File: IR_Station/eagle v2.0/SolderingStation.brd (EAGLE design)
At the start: 160 x 100 mm, 104 parts, among them IC1 LM317, U1 MSP340G2443, U2 UPD166010, U3 MCP6V08, U4 UPD166010, U5 MCP6V08, U6 ADS1115IDGST

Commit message: Update linse from all pins! some features :)
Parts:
- added C15, C8: 1nF, adi_v1.2:0805
- added JP11: (no value), pinhead:1X02
- added JP15: (no value), pinhead:1X01
- added JP16: (no value), pinhead:1X05
- added R25: 87R, adi_v1.2:0805
- added R34: 0R, adi_v1.2:0805
- added U$12: (no value), Serghei IR station:UNDEF1
- JP1: device pinhead:1X04/90 -> pinhead:1X02
- JP6: device pinhead:1X06 -> pinhead:1X04
- moved JP1 16.3 mm to (75.2, 80.8), turned to 90 degrees
- moved LED1 3.90 mm to (77.0, 76.5), turned to 180 degrees
- moved R21 3.15 mm to (75.9, 85.3)
- moved JP6 2.51 mm to (57.0, 23.0)
- moved R19 2.31 mm to (78.8, 81.8), turned to 90 degrees
- moved R9 1.80 mm to (82.1, 81.8)
- moved JP7 0.71 mm to (54.4, 45.5)
- moved JP10 0.50 mm to (64.2, 45.5)
- moved JP9 0.50 mm to (83.0, 45.5)
- moved R18 0.50 mm to (64.0, 42.7)
- moved U1 0.50 mm to (67.3, 31.8)
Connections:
- new net N$2222: JP1.1, LED1.A
- new net N$37: C8.1, U$12.P$2, U1.6
- new net N$39: C15.1, U$12.P$1, U1.7
- new net N$45: JP15.1, R25.1
- new net N$46: CLH1.INPUT, R34.1
- net +3V3_220V: now also JP16.2; no longer JP1.1
- net 24V_CS_UC: now also JP6.4; no longer JP6.6
- net 24V_PWM: now also R25.2, R34.2; no longer CLH1.INPUT
- net DATA_DISPLAY: now also JP6.1; no longer JP6.3
- net GND_220V: now also JP16.5; no longer JP1.4
- net GND_UC: now also C15.2, C8.2
- net N$15: now also JP16.4; no longer JP1.3
- net N$17: now also JP1.2, JP16.1; no longer LED1.A
- net N$36: now also JP16.3; no longer JP1.2
- net RX: now also JP6.3; no longer JP6.5
- net TIP_TEMP1_UC: now also JP11.2, U$12.P$3; no longer JP6.2, U1.6
- net TIP_TEMP2_UC: now also JP11.1, U$12.P$4; no longer JP6.1, U1.7
- net TX: now also JP6.2; no longer JP6.4
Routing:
- net N$37: track 0.00 -> 17.7 mm
- net N$39: track 0.00 -> 15.3 mm
- net N$17: track 4.49 -> 17.8 mm
- net N$46: track 0.00 -> 10.6 mm
- net N$26: track 180.0 -> 170.0 mm
- net TIP_TEMP1_UC: track 7.35 -> 3.31 mm
- net N$17_UC: track 0.00 -> 3.25 mm, vias 0 -> 2
- net N$2222: track 0.00 -> 2.96 mm
- net N$45: track 0.00 -> 2.65 mm
- net TIP_TEMP2_UC: track 6.08 -> 4.03 mm
- net N$25: track 102.0 -> 103.8 mm
- net +3V3_UC: track 106.1 -> 107.7 mm
- net N$10: track 16.0 -> 14.5 mm
- net GND_ST_LIPIT: track 168.3 -> 169.8 mm
- net N$6: track 8.49 -> 7.21 mm
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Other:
- board text added: "FRONT"
- board text added: "LED"
- board text added: "PANEL"
- board text added: "PWM_220V_LED"

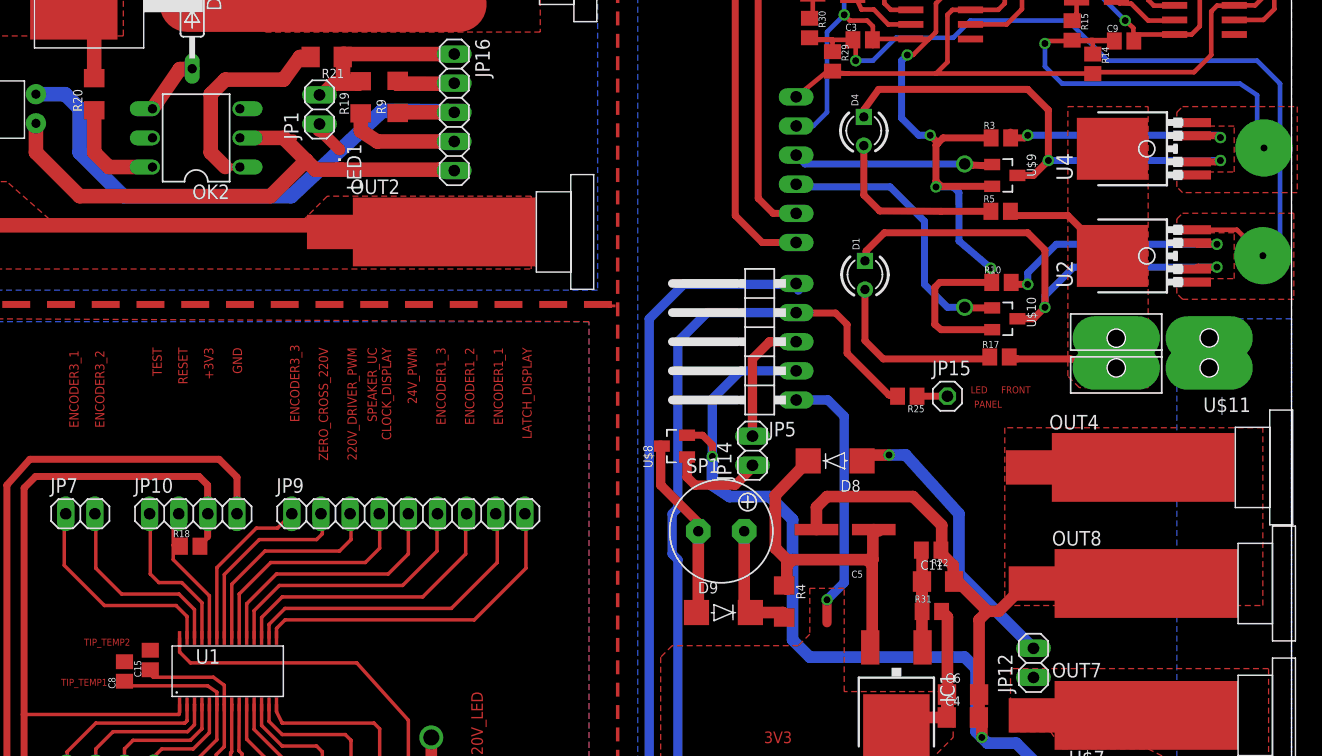
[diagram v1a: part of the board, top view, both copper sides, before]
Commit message: PDF, and correct few lines.
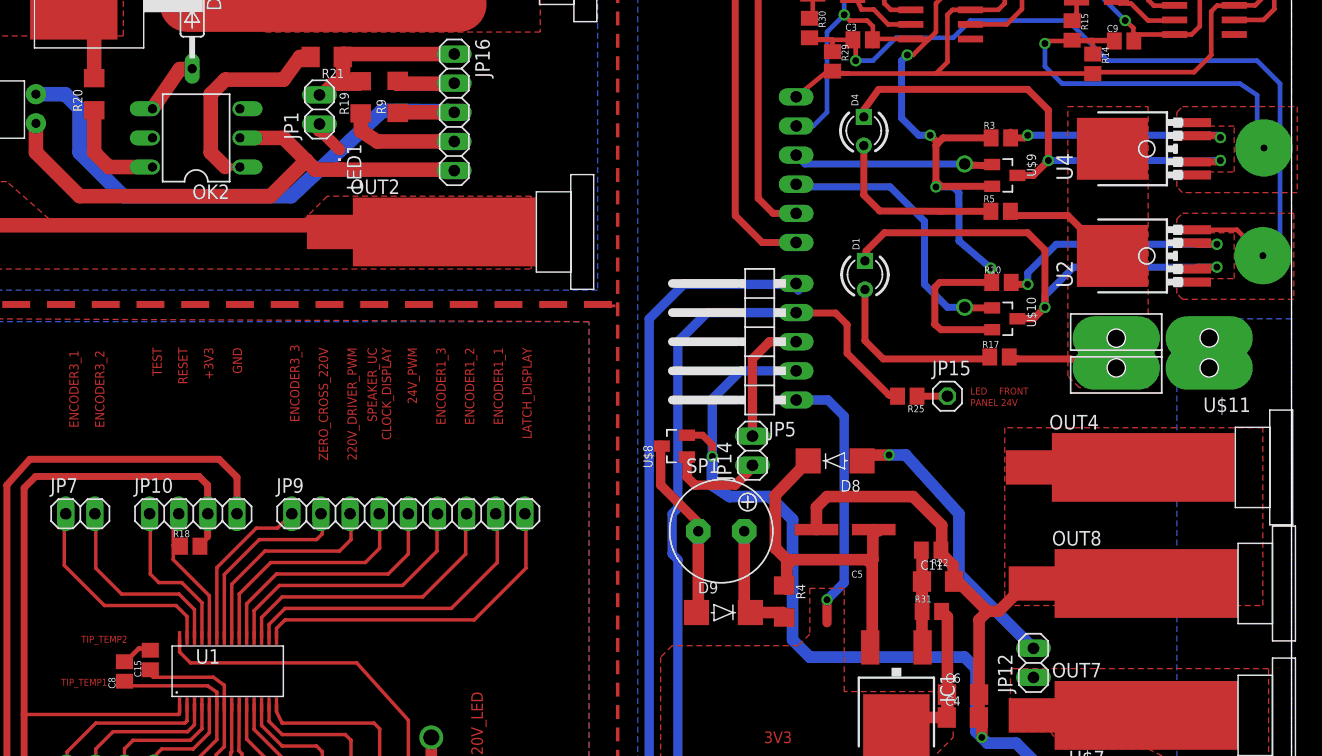
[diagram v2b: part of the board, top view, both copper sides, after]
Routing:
- net GND_UC: track 154.6 -> 157.5 mm
- net GND_220V: track 52.7 -> 52.0 mm
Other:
- board text added: "PANEL 24V"
- board text removed: "PANEL"
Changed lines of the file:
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@@
 <layer number="14" name="Route14" color="1" fill="6" visible="yes" active="yes"/>
 <layer number="15" name="Route15" color="4" fill="6" visible="yes" active="yes"/>
-<layer number="16" name="Bottom" color="1" fill="1" visible="yes" active="yes"/>
+<layer number="16" name="Bottom" color="1" fill="1" visible="no" active="yes"/>
 <layer number="17" name="Pads" color="2" fill="1" visible="yes" active="yes"/>
 <layer number="18" name="Vias" color="2" fill="1" visible="yes" active="yes"/>
@@
 <rectangle x1="0" y1="31" x2="44.25" y2="64" layer="16"/>
 <text x="56.75" y="30.5" size="0.6096" layer="1" font="vector" align="bottom-right">TIP_TEMP1</text>
-<text x="58.75" y="34" size="0.6096" layer="1" font="vector" align="bottom-right">TIP_TEMP2</text>
-<text x="133.5" y="56" size="0.6096" layer="1" font="vector" align="bottom-right">LED</text>
-<text x="137.25" y="56" size="0.6096" layer="1" font="vector" align="bottom-right">FRONT</text>
-<text x="134.75" y="54.75" size="0.6096" layer="1" font="vector" align="bottom-right">PANEL</text>
+<text x="58.5" y="34.25" size="0.6096" layer="1" font="vector" align="bottom-right">TIP_TEMP2</text>
+<text x="132" y="56.5" size="0.6096" layer="1" font="vector" rot="R180" align="bottom-right">LED</text>
+<text x="134.5" y="56.5" size="0.6096" layer="1" font="vector" rot="R180" align="bottom-right">FRONT</text>
+<text x="132" y="55.5" size="0.6096" layer="1" font="vector" rot="R180" align="bottom-right">PANEL 24V</text>
 <text x="89.5" y="30" size="1.016" layer="1" font="vector" rot="R90" align="bottom-right">PWM_220V_LED</text>
 </plain>
@@
 <wire x1="155.5" y1="83" x2="157" y2="82" width="0.4064" layer="16"/>
 <wire x1="157" y1="82" x2="157" y2="78" width="0.4064" layer="16"/>
-<wire x1="157" y1="78" x2="157.5" y2="77.5" width="0.4064" layer="16"/>
-<wire x1="157.6" y1="77.4" x2="157.5" y2="77.5" width="0" layer="19" extent="16-16"/>
+<wire x1="157" y1="78" x2="157.6" y2="77.4" width="0.4064" layer="16"/>
 </signal>
 <signal name="N$2">
@@
 <wire x1="68.31" y1="78.27" x2="72.12" y2="78.27" width="1.27" layer="1"/>
 <wire x1="72.12" y1="78.27" x2="74.0885" y2="76.3015" width="1.27" layer="1"/>
-<wire x1="72.12" y1="78.27" x2="73.021" y2="78.27" width="0.6096" layer="1"/>
+<wire x1="72.12" y1="78.27" x2="72.271" y2="78.27" width="0.6096" layer="1"/>
 <wire x1="87.17" y1="75.52" x2="85.75" y2="75.5" width="1.27" layer="1"/>
 <wire x1="85.75" y1="75.5" x2="74.89" y2="75.5" width="1.27" layer="1"/>
@@
 <wire x1="119.55" y1="84.09" x2="116.81" y2="81.85" width="0.4064" layer="1"/>
 <wire x1="130" y1="84.88" x2="129" y2="83.88" width="0.4064" layer="1"/>
-<wire x1="119.98" y1="84.09" x2="120" y2="84" width="0" layer="19" extent="1-1"/>
+<wire x1="120" y1="84" x2="120" y2="84.07" width="0.4064" layer="1"/>
+<wire x1="120" y1="84.07" x2="119.98" y2="84.09" width="0.4064" layer="1"/>
 </signal>
 <signal name="+12V">
@@
 <wire x1="108.28" y1="44.72" x2="105" y2="48" width="0.8128" layer="1"/>
 <wire x1="105" y1="48" x2="105" y2="51.5" width="0.8128" layer="1"/>
-<wire x1="105" y1="51.5" x2="105.1" y2="51.4" width="0" layer="19" extent="1-1"/>
+<wire x1="105" y1="51.5" x2="105.1" y2="51.4" width="0.4064" layer="1"/>
 </signal>
 <signal name="SPEAKER">
@@
 <wire x1="112.82" y1="36.89" x2="115.66" y2="36.89" width="1.016" layer="1"/>
 <wire x1="115.66" y1="36.89" x2="115.77" y2="36.45" width="1.016" layer="1"/>
-<wire x1="112.82" y1="36.89" x2="113" y2="37" width="0" layer="19" extent="1-1"/>
+<wire x1="113" y1="37" x2="112.93" y2="37" width="0.4064" layer="1"/>
+<wire x1="112.93" y1="37" x2="112.82" y2="36.89" width="0.4064" layer="1"/>
 </signal>
 <signal name="24V_PWM_UC">
@@
 <contactref element="C8" pad="2"/>
 <contactref element="C15" pad="2"/>
-<wire x1="60.5" y1="33.6" x2="58.25" y2="32.6" width="0" layer="19" extent="1-1"/>
+<wire x1="58.25" y1="32.6" x2="58.35" y2="32.6" width="0.4064" layer="1"/>
+<wire x1="58.35" y1="32.6" x2="59.5" y2="33.75" width="0.4064" layer="1"/>
+<wire x1="59.5" y1="33.75" x2="60.25" y2="33.75" width="0.4064" layer="1"/>
+<wire x1="60.25" y1="33.75" x2="60.5" y2="33.5" width="0.4064" layer="1"/>
+<wire x1="60.5" y1="33.6" x2="60.5" y2="33.5" width="0.4064" layer="1"/>
 </signal>
 <signal name="+3V3_UC">
@@
 <wire x1="66.30365" y1="29.94635" x2="65.5" y2="30.5" width="0.3048" layer="1"/>
 <wire x1="65.5" y1="30.5" x2="58.25" y2="30.5" width="0.3048" layer="1"/>
-<wire x1="58.25" y1="30.5" x2="58.25" y2="31" width="0.3048" layer="1"/>
-<wire x1="58.25" y1="31" x2="58.25" y2="30.9" width="0" layer="19" extent="1-1"/>
+<wire x1="58.25" y1="30.5" x2="58.25" y2="30.9" width="0.3048" layer="1"/>
+<wire x1="58.25" y1="31" x2="58.25" y2="30.9" width="0.4064" layer="1"/>
 </signal>
 <signal name="N$39">
